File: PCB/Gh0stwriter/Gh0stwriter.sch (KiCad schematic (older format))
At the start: 20 parts, among them J1 Conn_01x06, J2 Conn_01x02, J3 Conn_01x06, J4 Conn_01x02, J5 Conn_01x06, J6 Conn_01x06, J7 Conn_01x02, Q1 Q_NPN_Darlington_ECB

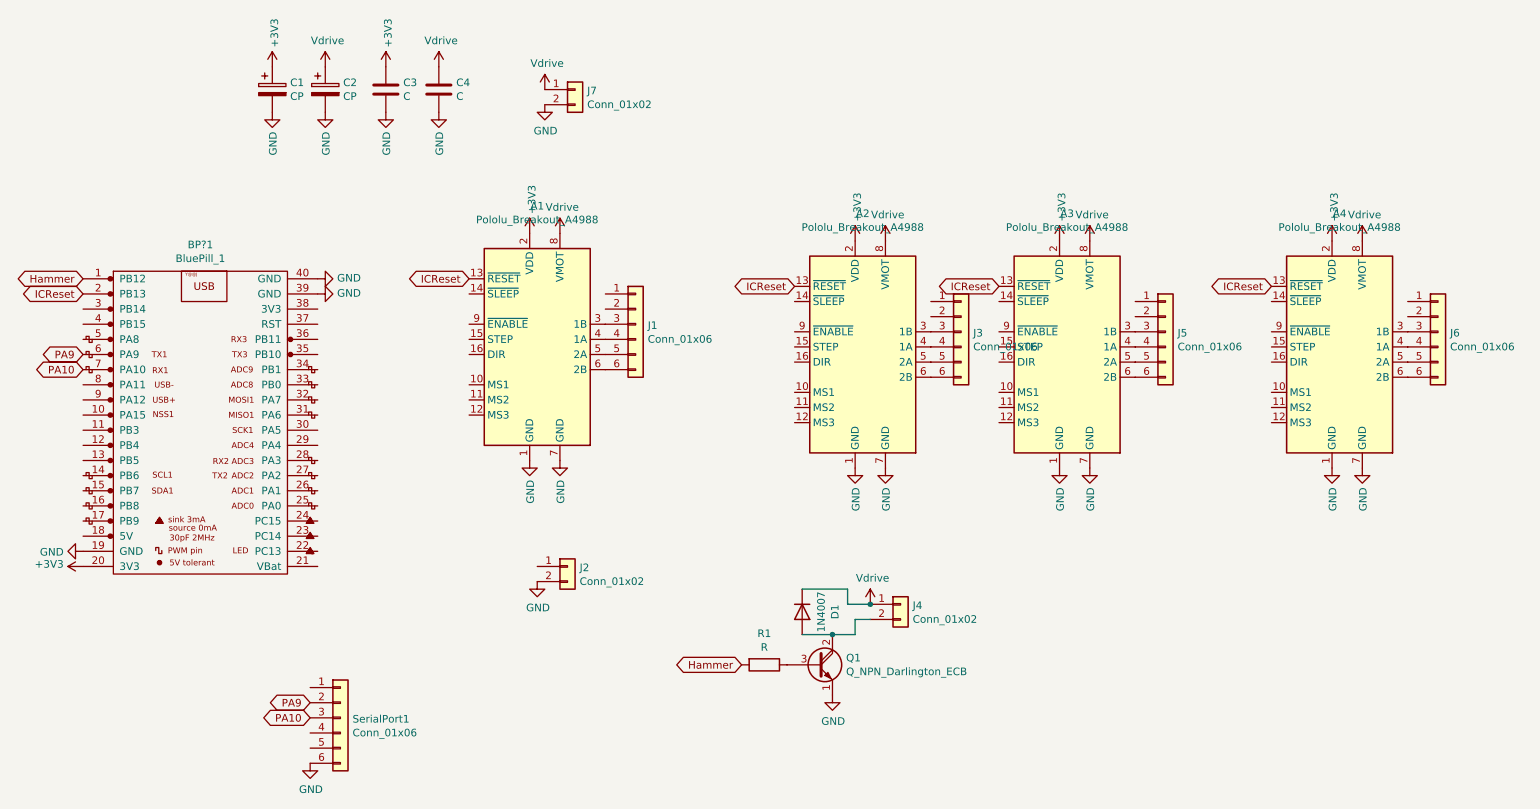
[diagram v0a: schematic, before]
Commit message: Serial comunication added
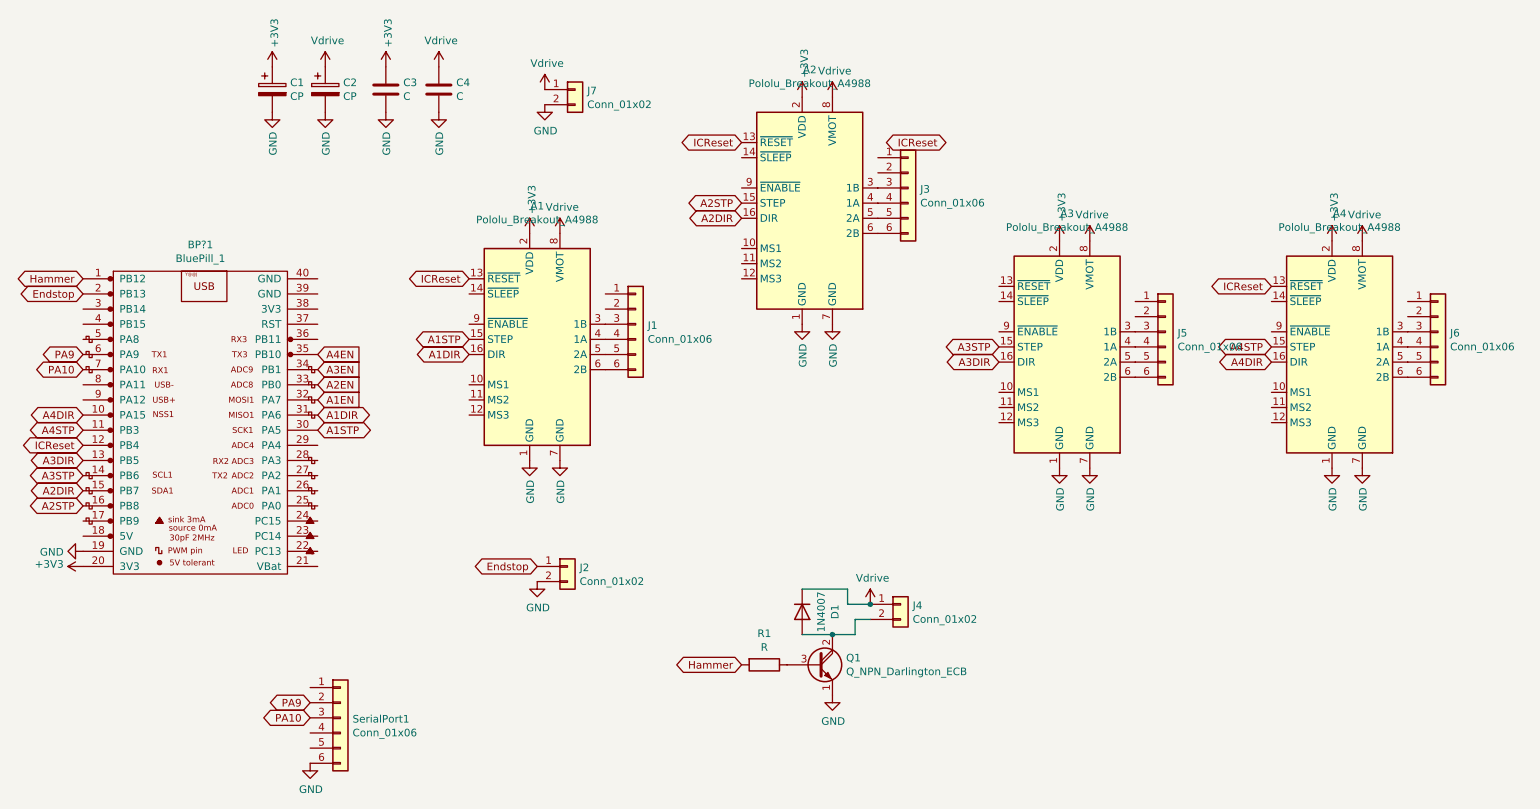
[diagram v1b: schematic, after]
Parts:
- C1, C2: footprint Capacitor_THT:CP_Radial_D8.0mm_P2.50mm -> Capacitor_THT:CP_Radial_D6.3mm_P2.50mm
- D1: footprint Diode_THT:D_DO-41_SOD81_P10.16mm_Horizontal -> Diode_THT:D_DO-35_SOD27_P2.54mm_Vertical_AnodeUp
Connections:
- net GND: no longer BP?1.39 (GND), BP?1.40 (GND)
- net ICReset: now also BP?1.12 (PB4); no longer A3.13 (~RESET), BP?1.2 (PB13)
- net A3STP: now reaches A3.15 (STEP)
- net A3STP: now also BP?1.14 (PB6)
- net A3DIR: now reaches A3.16 (DIR)
- net A3DIR: now also BP?1.13 (PB5)
- net A4DIR: now reaches BP?1.10 (PA15)
- net A4DIR: now also A4.16 (DIR)
- net A4STP: now reaches BP?1.11 (PB3)
- net A4STP: now also A4.15 (STEP)
- net A2DIR: now reaches BP?1.15 (PB7)
- net A2DIR: now also A2.16 (DIR)
- net A2STP: now reaches BP?1.16 (PB8)
- net A2STP: now also A2.15 (STEP)
- net A1STP: now reaches BP?1.30 (PA5)
- net A1STP: now also A1.15 (STEP)
- net A1DIR: now reaches BP?1.31 (PA6)
- net A1DIR: now also A1.16 (DIR)
- net A1EN: now reaches BP?1.32 (PA7)
- net A2EN: now reaches BP?1.33 (PB0)
- net A3EN: now reaches BP?1.34 (PB1)
- net A4EN: now reaches BP?1.35 (PB10)
- net Endstop: now reaches J2.1 (Pin_1)
- net Endstop: now also BP?1.2 (PB13)
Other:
- moved on the sheet: A2, J3
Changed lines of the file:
@@
 L Driver_Motor:Pololu_Breakout_A4988 A2
 U 1 1 5ECFA6AE
-P 6250 4250
-F 0 "A2" H 6300 5131 50  0000 C CNN
-F 1 "Pololu_Breakout_A4988" H 6300 5040 50  0000 C CNN
-F 2 "Module:Pololu_Breakout-16_15.2x20.3mm" H 6525 3500 50  0001 L CNN
-F 3 "https://www.pololu.com/product/2980/pictures" H 6350 3950 50  0001 C CNN
-	1    6250 4250
+P 5900 3300
+F 0 "A2" H 5950 4181 50  0000 C CNN
+F 1 "Pololu_Breakout_A4988" H 5950 4090 50  0000 C CNN
+F 2 "Module:Pololu_Breakout-16_15.2x20.3mm" H 6175 2550 50  0001 L CNN
+F 3 "https://www.pololu.com/product/2980/pictures" H 6000 3000 50  0001 C CNN
+	1    5900 3300
 	1    0    0    -1
 $EndComp
@@
 F 0 "D1" H 5900 6217 50  0000 C CNN
 F 1 "1N4007" H 5900 6126 50  0000 C CNN
-F 2 "Diode_THT:D_DO-41_SOD81_P10.16mm_Horizontal" H 5900 5825 50  0001 C CNN
+F 2 "Diode_THT:D_DO-35_SOD27_P2.54mm_Vertical_AnodeUp" H 5900 5825 50  0001 C CNN
 F 3 "http://www.vishay.com/docs/88503/1n4001.pdf" H 5900 6000 50  0001 C CNN
 	1    5900 6000
@@
 F 0 "C2" H 2868 2596 50  0000 L CNN
 F 1 "CP" H 2868 2505 50  0000 L CNN
-F 2 "Capacitor_THT:CP_Radial_D8.0mm_P2.50mm" H 2788 2400 50  0001 C CNN
+F 2 "Capacitor_THT:CP_Radial_D6.3mm_P2.50mm" H 2788 2400 50  0001 C CNN
 F 3 "~" H 2750 2550 50  0001 C CNN
 	1    2750 2550
@@
 F 0 "C1" H 2518 2596 50  0000 L CNN
 F 1 "CP" H 2518 2505 50  0000 L CNN
-F 2 "Capacitor_THT:CP_Radial_D8.0mm_P2.50mm" H 2438 2400 50  0001 C CNN
+F 2 "Capacitor_THT:CP_Radial_D6.3mm_P2.50mm" H 2438 2400 50  0001 C CNN
 F 3 "~" H 2400 2550 50  0001 C CNN
 	1    2400 2550
@@
 	1    2850 6700
 	1    0    0    -1
-$EndComp
-$Comp
-L power:GND #PWR0101
-U 1 1 5ED48418
-P 2700 3800
-F 0 "#PWR0101" H 2700 3550 50  0001 C CNN
-F 1 "GND" V 2705 3672 50  0000 R CNN
-F 2 "" H 2700 3800 50  0001 C CNN
-F 3 "" H 2700 3800 50  0001 C CNN
-	1    2700 3800
-	0    -1   -1   0
-$EndComp
-$Comp
-L power:GND #PWR0102
-U 1 1 5ED4AAB5
-P 2700 3900
-F 0 "#PWR0102" H 2700 3650 50  0001 C CNN
-F 1 "GND" V 2705 3772 50  0000 R CNN
-F 2 "" H 2700 3900 50  0001 C CNN
-F 3 "" H 2700 3900 50  0001 C CNN
-	1    2700 3900
-	0    -1   -1   0
 $EndComp
 $Comp
@@
 L power:GND #PWR0111
 U 1 1 5ED7A1C8
-P 6250 5050
-F 0 "#PWR0111" H 6250 4800 50  0001 C CNN
-F 1 "GND" V 6255 4922 50  0000 R CNN
-F 2 "" H 6250 5050 50  0001 C CNN
-F 3 "" H 6250 5050 50  0001 C CNN
-	1    6250 5050
+P 5900 4100
+F 0 "#PWR0111" H 5900 3850 50  0001 C CNN
+F 1 "GND" V 5905 3972 50  0000 R CNN
+F 2 "" H 5900 4100 50  0001 C CNN
+F 3 "" H 5900 4100 50  0001 C CNN
+	1    5900 4100
 	1    0    0    -1
 $EndComp
@@
 L power:GND #PWR0112
 U 1 1 5ED7A4BD
-P 6450 5050
-F 0 "#PWR0112" H 6450 4800 50  0001 C CNN
-F 1 "GND" V 6455 4922 50  0000 R CNN
-F 2 "" H 6450 5050 50  0001 C CNN
-F 3 "" H 6450 5050 50  0001 C CNN
-	1    6450 5050
+P 6100 4100
+F 0 "#PWR0112" H 6100 3850 50  0001 C CNN
+F 1 "GND" V 6105 3972 50  0000 R CNN
+F 2 "" H 6100 4100 50  0001 C CNN
+F 3 "" H 6100 4100 50  0001 C CNN
+	1    6100 4100
 	1    0    0    -1
 $EndComp
@@
 L power:+3V3 #PWR0118
 U 1 1 5ED85A0B
-P 6250 3550
-F 0 "#PWR0118" H 6250 3400 50  0001 C CNN
-F 1 "+3V3" V 6265 3678 50  0000 L CNN
-F 2 "" H 6250 3550 50  0001 C CNN
-F 3 "" H 6250 3550 50  0001 C CNN
-	1    6250 3550
+P 5900 2600
+F 0 "#PWR0118" H 5900 2450 50  0001 C CNN
+F 1 "+3V3" V 5915 2728 50  0000 L CNN
+F 2 "" H 5900 2600 50  0001 C CNN
+F 3 "" H 5900 2600 50  0001 C CNN
+	1    5900 2600
 	1    0    0    -1
 $EndComp
@@
 L power:Vdrive #PWR0124
 U 1 1 5EDBB3D5
-P 6450 3550
-F 0 "#PWR0124" H 6250 3400 50  0001 C CNN
-F 1 "Vdrive" H 6465 3723 50  0000 C CNN
-F 2 "" H 6450 3550 50  0001 C CNN
-F 3 "" H 6450 3550 50  0001 C CNN
-	1    6450 3550
+P 6100 2600
+F 0 "#PWR0124" H 5900 2450 50  0001 C CNN
+F 1 "Vdrive" H 6115 2773 50  0000 C CNN
+F 2 "" H 6100 2600 50  0001 C CNN
+F 3 "" H 6100 2600 50  0001 C CNN
+	1    6100 2600
 	1    0    0    -1
 $EndComp
@@
 Text GLabel 3700 3800 0    50   BiDi ~ 0
 ICReset
-Text GLabel 5850 3850 0    50   BiDi ~ 0
+Text GLabel 5500 2900 0    50   BiDi ~ 0
 ICReset
-Text GLabel 7200 3850 0    50   BiDi ~ 0
+Text GLabel 6850 2900 0    50   BiDi ~ 0
 ICReset
 Text GLabel 9000 3850 0    50   BiDi ~ 0
 ICReset
-Text GLabel 1150 3900 0    50   BiDi ~ 0
+Text GLabel 1150 4900 0    50   BiDi ~ 0
 ICReset
 $Comp
 L Connector_Generic:Conn_01x06 J3
 U 1 1 5EE5F861
-P 6950 4150
-F 0 "J3" H 7030 4142 50  0000 L CNN
-F 1 "Conn_01x06" H 7030 4051 50  0000 L CNN
-F 2 "Connector_JST:JST_XH_B6B-XH-A_1x06_P2.50mm_Vertical" H 6950 4150 50  0001 C CNN
-F 3 "~" H 6950 4150 50  0001 C CNN
-	1    6950 4150
+P 6600 3200
+F 0 "J3" H 6680 3192 50  0000 L CNN
+F 1 "Conn_01x06" H 6680 3101 50  0000 L CNN
+F 2 "Connector_JST:JST_XH_B6B-XH-A_1x06_P2.50mm_Vertical" H 6600 3200 50  0001 C CNN
+F 3 "~" H 6600 3200 50  0001 C CNN
+	1    6600 3200
 	1    0    0    -1
 $EndComp
@@
 Text GLabel 5500 6350 0    50   BiDi ~ 0
 Hammer
+Text GLabel 4150 5700 0    50   BiDi ~ 0
+Endstop
+Text GLabel 1150 3900 0    50   BiDi ~ 0
+Endstop
+Text GLabel 1150 4700 0    50   BiDi ~ 0
+A4DIR
+Text GLabel 1150 4800 0    50   BiDi ~ 0
+A4STP
+Text GLabel 9000 4250 0    50   BiDi ~ 0
+A4STP
+Text GLabel 9000 4350 0    50   BiDi ~ 0
+A4DIR
+Text GLabel 7200 4250 0    50   BiDi ~ 0
+A3STP
+Text GLabel 7200 4350 0    50   BiDi ~ 0
+A3DIR
+Text GLabel 5500 3300 0    50   BiDi ~ 0
+A2STP
+Text GLabel 5500 3400 0    50   BiDi ~ 0
+A2DIR
+Text GLabel 3700 4200 0    50   BiDi ~ 0
+A1STP
+Text GLabel 3700 4300 0    50   BiDi ~ 0
+A1DIR
+Text GLabel 1150 5000 0    50   BiDi ~ 0
+A3DIR
+Text GLabel 1150 5100 0    50   BiDi ~ 0
+A3STP
+Text GLabel 1150 5200 0    50   BiDi ~ 0
+A2DIR
+Text GLabel 1150 5300 0    50   BiDi ~ 0
+A2STP
+Text GLabel 2700 4700 2    50   BiDi ~ 0
+A1DIR
+Text GLabel 2700 4800 2    50   BiDi ~ 0
+A1STP
+Text GLabel 2700 4600 2    50   Input ~ 0
+A1EN
+Text GLabel 2700 4500 2    50   Input ~ 0
+A2EN
+Text GLabel 2700 4400 2    50   Input ~ 0
+A3EN
+Text GLabel 2700 4300 2    50   Input ~ 0
+A4EN
 $EndSCHEMATC
